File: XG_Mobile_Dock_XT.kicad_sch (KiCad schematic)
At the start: 33 parts, among them J1 5-1775443-8, J13 39301240, J14 I2C1, J2 20455-040E-76, J3 20455-040E-76, J5 USB_C_Receptacle, J6 455860005, J7 10147430-113T0LF, SW1 SW_Push

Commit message: ported more changes from previous version
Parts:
- added C49, C54: 10uF, Capacitor_SMD:C_0603_1608Metric, symbol Device:C
- added Q1: ~, MMBT5551 RANGE 200-300:SOT-23-3_L2.9-W1.3-P1.90-LS2.4-BR, symbol MMBT5551 RANGE 200-300:MMBT5551_C2145
- added R111: 4k, Resistor_SMD:R_0603_1608Metric, symbol Device:R
- added R112: 100, Resistor_SMD:R_0603_1608Metric, symbol Device:R
- added SW30, SW31: ~, DSWB02LHGET:SW-TH_DSWB02LHGET, symbol DSWB02LHGET:DSWB02LHGET
- added U5: ~, LD1086DT33TR:TO-252-2_L6.5-W6.1-P4.58-LS10.0-TL, symbol LD1086DT33TR:LD1086DT33TR
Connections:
- net +3V3: now also SW31.2
- net GND: now also C49.1, C54.1, Q1.2 (E), SW30.4, U5.1 (GND); no longer J13.16
- net PSPWROK: now reaches J13.8
- net +5VSB: now reaches J13.9
- net +5VSB: now also C49.2, U5.3 (IN)
- new net: J13.16, SW30.1, SW30.2
- new net: R112.1, SW30.3
- new net: Q1.1 (B), R111.2
- new net: Q1.3 (C), R112.2
- new net +3V3MCU: SW31.3, SW31.4
- new net +3V3SB: C54.2, SW31.1, U5.4 (OUT)
- new net PSON: R111.1
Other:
- sheet MCU ports: added PB2, PB7; removed none
- note added: "100nF GRM033R61C104KE84D MfPart C76937 LCSC 220nF GRM033R61C224KE14D MfPart C161474 LCSC 1uf CL03A105MO3NRNH MfPart C307385 LCSC 1k RC0603JR-071KL MfPart C14676 LCSC L0 8.25k 0603WAF8251T5E MfPart C23113 LCSC L1 24.9k RC0603FR-0724K9L MfPart C137761 LCSC L2 75k 0603WAF7502T5E MfPart C23242 LCSC L3 4.7k 0402WGF4701TCE MfPart C25900 LCSC 0402 10 0603WAF100JT5E MfPart C22859 LCSC 0603 4.02k 0603WAF4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"
- note removed: "100nF GRM033R61C104KE84D MfPart C76937 LCSC 220nF GRM033R61C224KE14D MfPart C161474 LCSC 1uf CL03A105MO3NRNH MfPart C307385 LCSC 1k RC0603JR-071KL MfPart C14676 LCSC L0 8.25k 0603WAF8251T5E MfPart C23113 LCSC L1 24.9k RC0603FR-0724K9L MfPart C137761 LCSC L2 75k 0603WAF7502T5E MfPart C23242 LCSC L3 4.7k 0402WGF4701TCE MfPart C25900 LCSC 0402"

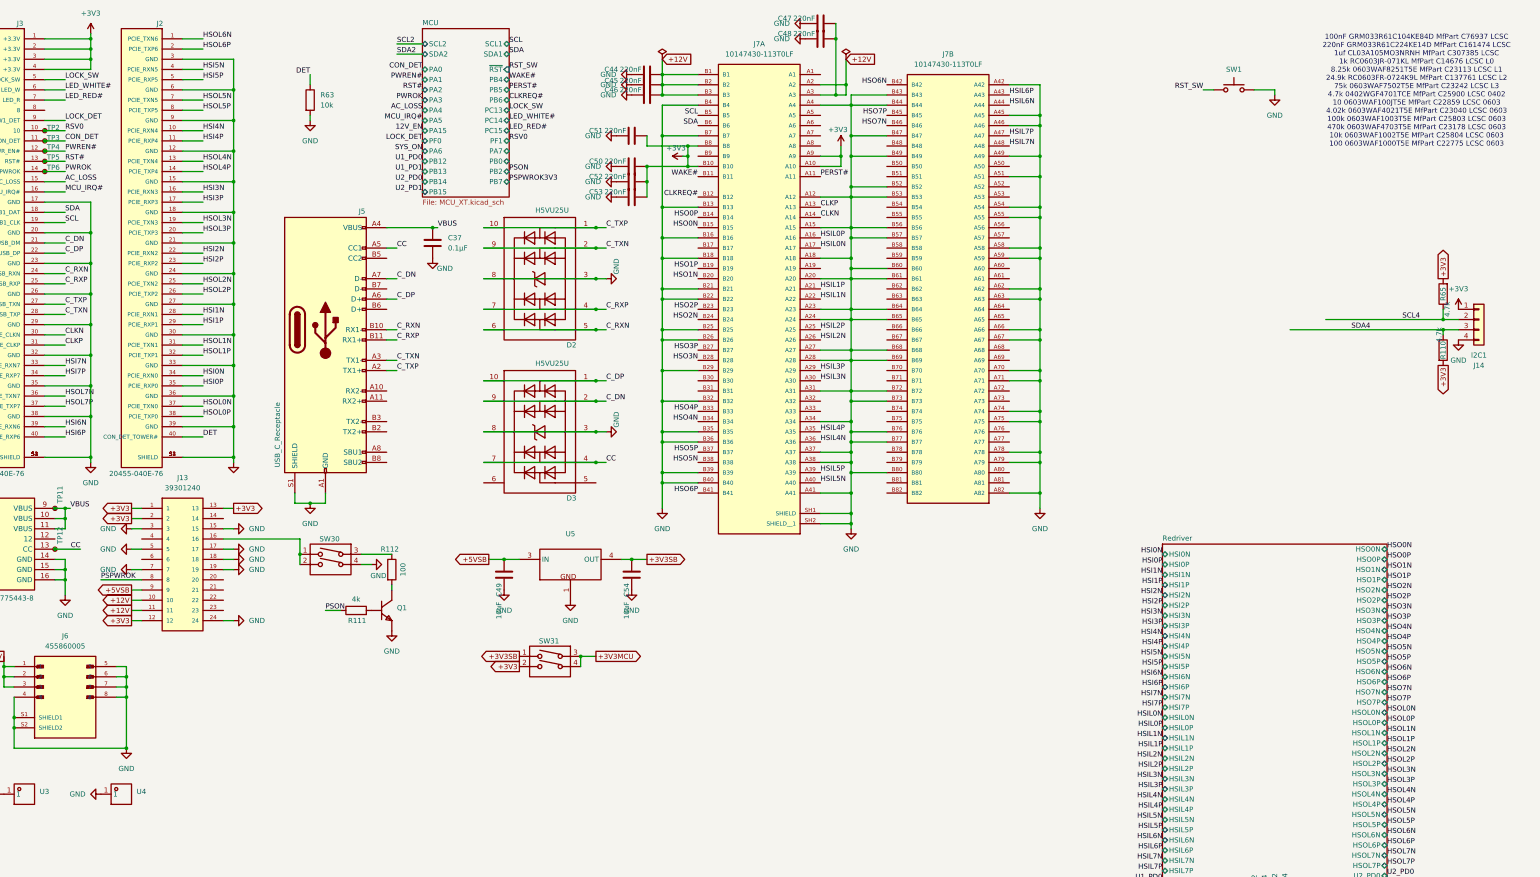
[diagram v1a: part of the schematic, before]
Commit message: added more missing functionality to start psu
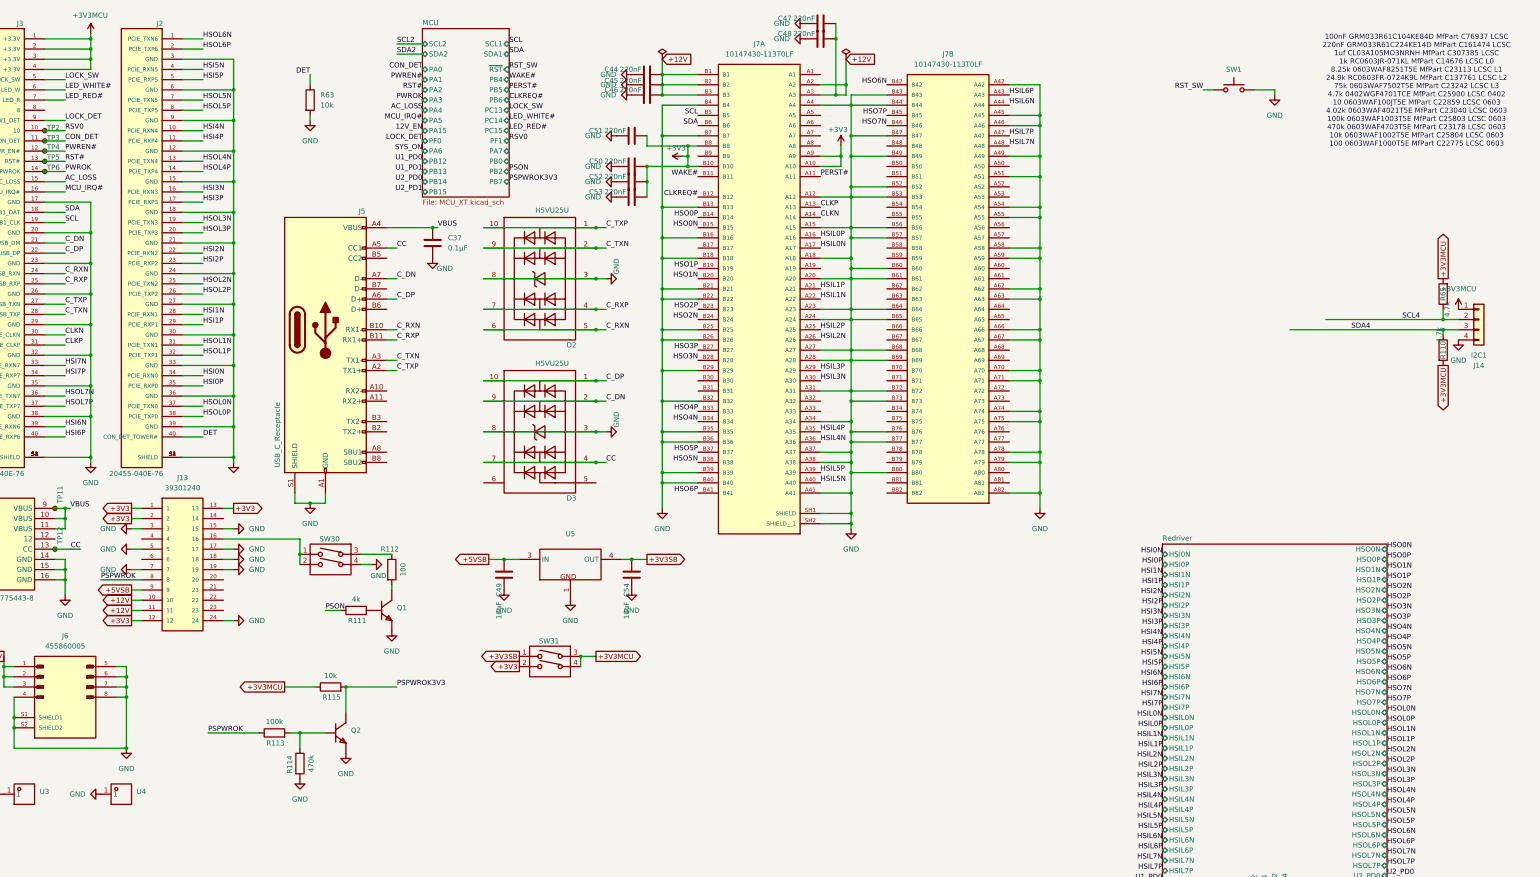
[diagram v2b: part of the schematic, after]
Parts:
- removed Q1: ~, MMBT5551 RANGE 200-300:SOT-23-3_L2.9-W1.3-P1.90-LS2.4-BR, symbol MMBT5551 RANGE 200-300:MMBT5551_C2145
- added Q1, Q2: ~, MMBT5551 RANGE 200-300:SOT-23-3_L2.9-W1.3-P1.90-LS2.4-BR, symbol MMBT5551(RANGE_200-300):MMBT5551_C2145
- added R113: 100k, Resistor_SMD:R_0603_1608Metric, symbol Device:R
- added R114: 470k, Resistor_SMD:R_0603_1608Metric, symbol Device:R
- added R115: 10k, Resistor_SMD:R_0603_1608Metric, symbol Device:R
- U5: LCSC C12051 -> (none); LCSC Part Name (none) -> 1.5 A可调与固定低压降正电压稳压器; Manufacturer Part (none) -> LD1086DT33TR; Part_Number LD1086DT33TR -> (none); Supplier (none) -> LCSC; Supplier Part (none) -> C12051
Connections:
- net +3V3: no longer J14.1 (Pin_1), J3.1 (+3.3V), J3.2 (+3.3V), J3.3 (+3.3V), J3.4 (+3.3V), R110.2, R65.2
- net +3V3MCU: now also J14.1 (Pin_1), J3.1 (+3.3V), J3.2 (+3.3V), J3.3 (+3.3V), J3.4 (+3.3V), R110.2, R65.2, R115.1
- net GND: now also Q1.2 (E), Q2.2 (E), R114.2
- net PSPWROK: now also R113.1
- net PSPWROK3V3: now also Q2.3 (C), R115.2
- net at R111.2: now also Q1.1 (B)
- net at R112.2: now also Q1.3 (C)
- new net: Q2.1 (B), R113.2, R114.1

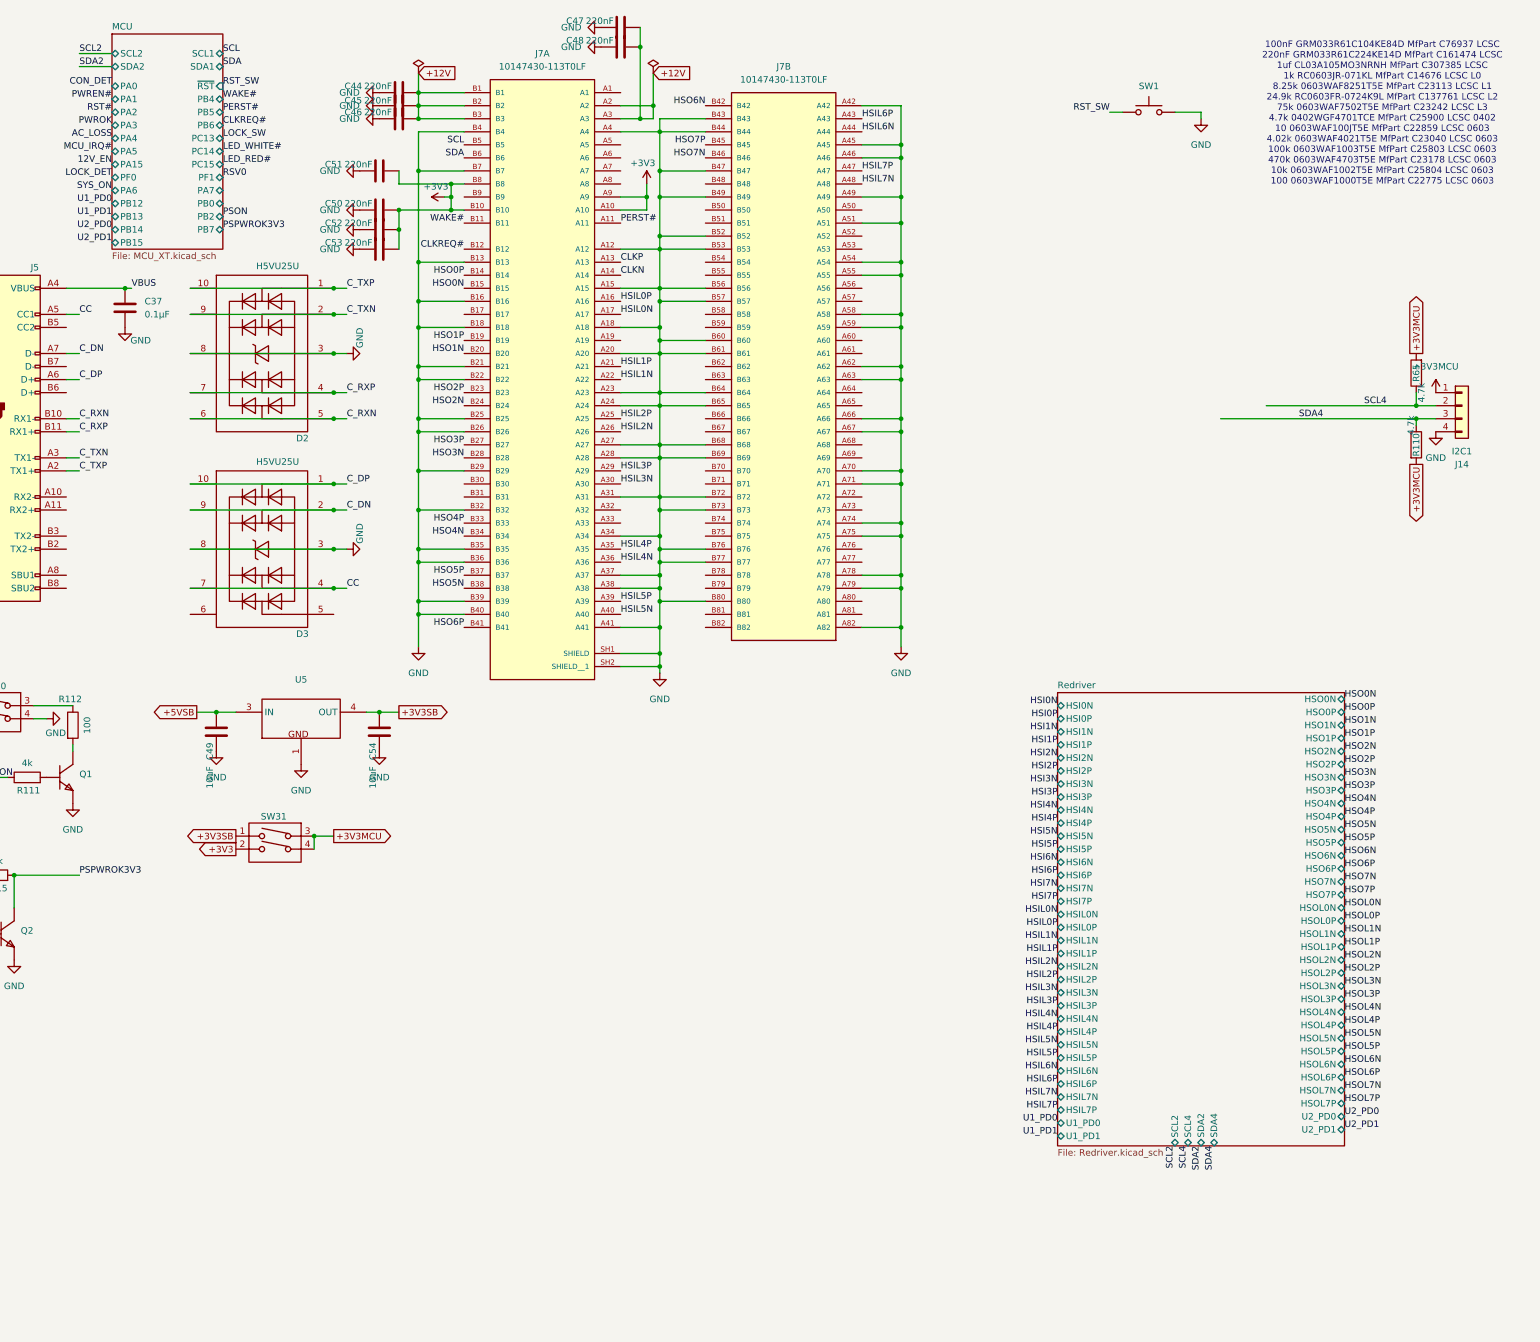
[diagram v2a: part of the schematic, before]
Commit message: started to add retimer for usb
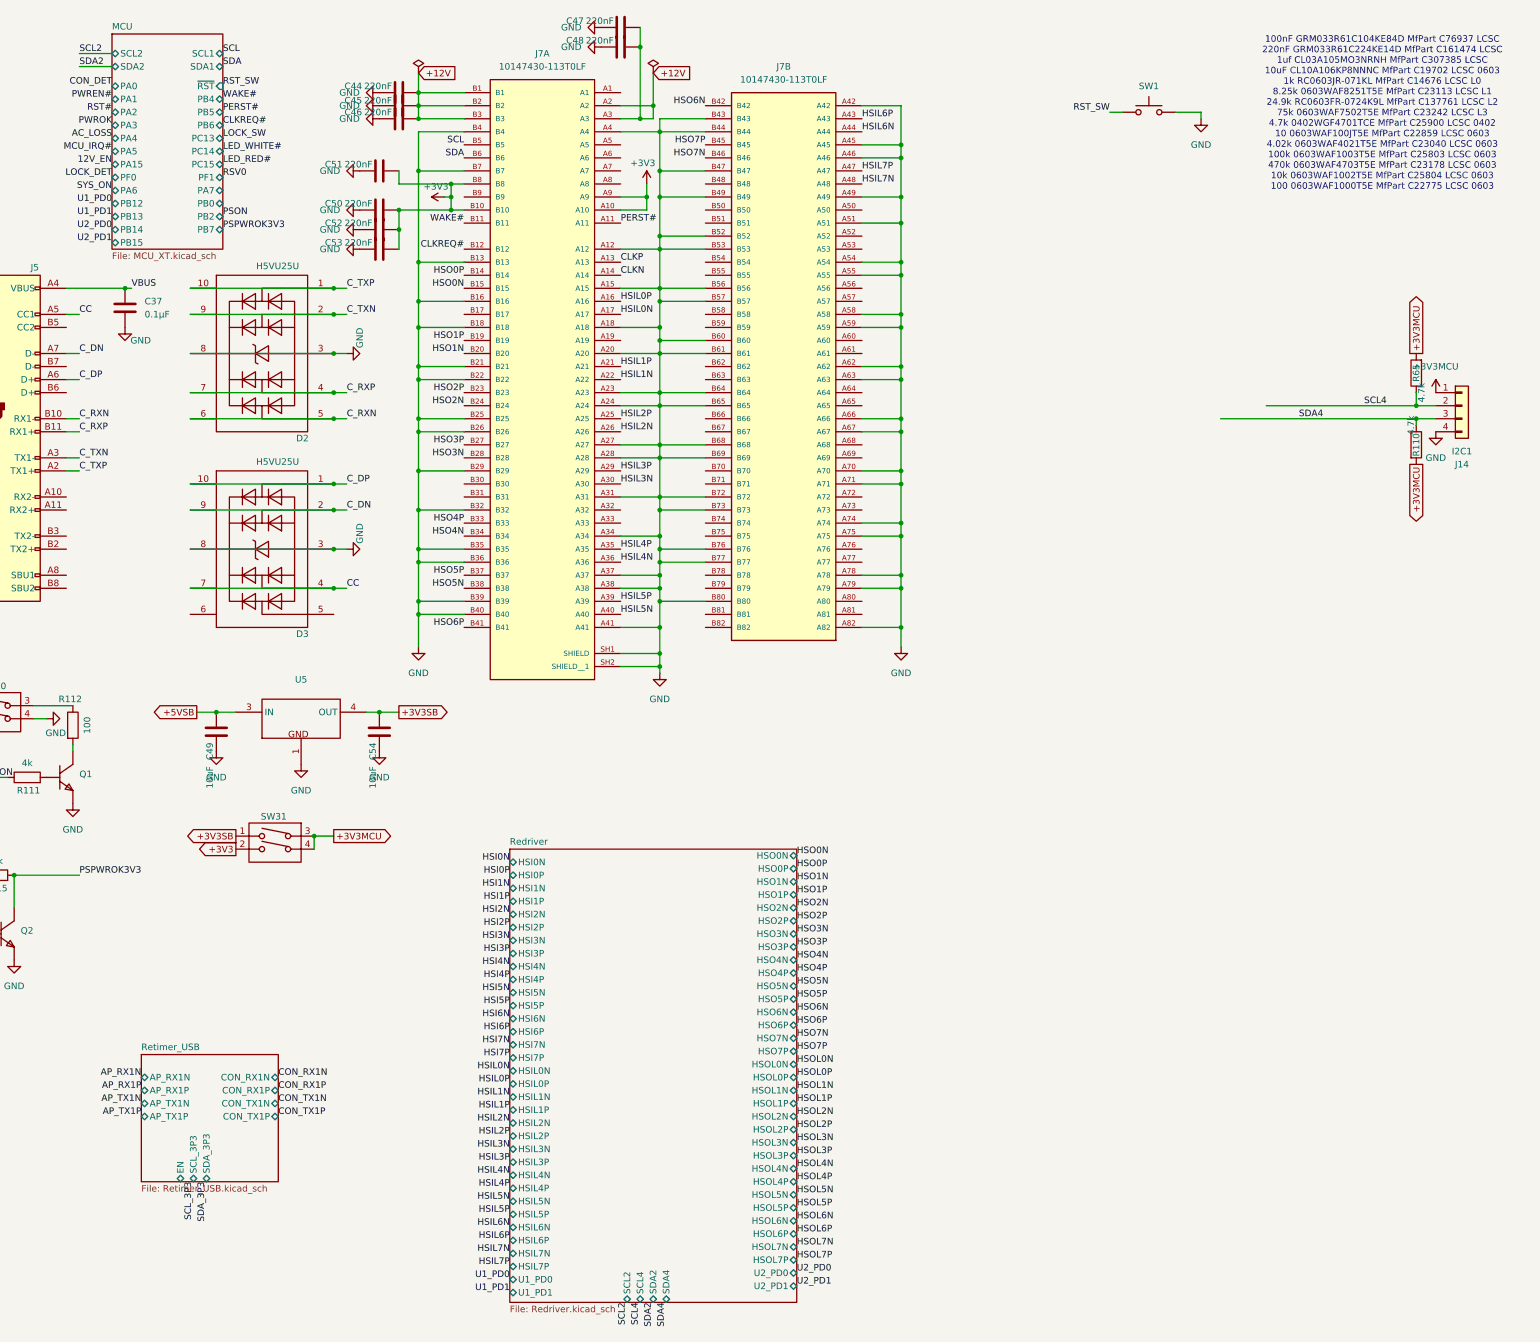
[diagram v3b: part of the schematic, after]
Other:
- added sheet Retimer_USB (Retimer_USB.kicad_sch)
- note added: "100nF GRM033R61C104KE84D MfPart C76937 LCSC 220nF GRM033R61C224KE14D MfPart C161474 LCSC 1uf CL03A105MO3NRNH MfPart C307385 LCSC 10uF CL10A106KP8NNNC MfPart C19702 LCSC 0603 1k RC0603JR-071KL MfPart C14676 LCSC L0 8.25k 0603WAF8251T5E MfPart C23113 LCSC L1 24.9k RC0603FR-0724K9L MfPart C137761 LCSC L2 75k 0603WAF7502T5E MfPart C23242 LCSC L3 4.7k 0402WGF4701TCE MfPart C25900 LCSC 0402 10 0603WAF1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"
- note removed: "100nF GRM033R61C104KE84D MfPart C76937 LCSC 220nF GRM033R61C224KE14D MfPart C161474 LCSC 1uf CL03A105MO3NRNH MfPart C307385 LCSC 1k RC0603JR-071KL MfPart C14676 LCSC L0 8.25k 0603WAF8251T5E MfPart C23113 LCSC L1 24.9k RC0603FR-0724K9L MfPart C137761 LCSC L2 75k 0603WAF7502T5E MfPart C23242 LCSC L3 4.7k 0402WGF4701TCE MfPart C25900 LCSC 0402 10 0603WAF100JT5E MfPart C22859 LCSC 0603 4.02k 0603WAF4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"
